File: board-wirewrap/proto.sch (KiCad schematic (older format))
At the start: 39 parts, among them P1 AB, P101 Data, P102 Power, P2 CD, SW101 RESET, U1 DS8641-LR, U101 Am2908, U102 Am2908, U103 Am2908, U104 Am2908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

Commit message: This matches the old indicator panels, the first batch before I changed them all around.
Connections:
- net +12V: now also P102.3 (P3), P102.4 (P4), P102.5 (P5), P102.6 (P6), P102.7 (P7), P102.8 (P8); no longer P102.1 (P1), P102.10 (P10), P102.2 (P2), P102.9 (P9)
- net GND: now also P102.1 (P1), P102.10 (P10), P102.2 (P2), P102.9 (P9); no longer P102.3 (P3), P102.4 (P4), P102.5 (P5), P102.6 (P6), P102.7 (P7), P102.8 (P8)
- net IPclk: now also P2.20 (D10)
- net IPdata: now also P2.22 (D11)
- net IPlatch: now also P2.24 (D12)
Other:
- note removed: "NOTES:\n\n1) Which signal goes to which package has not yet\n been fixed. Will be done during PCB layout.\n2) Do we need to tie the unconnected bus lines on\n the DS8641s to +5V?"
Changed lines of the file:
@@
 Text Label 6200 8050 2    60   ~ 0
 BDAL21
-Text Notes 3000 6750 0    60   ~ 0
-NOTES:\n\n1) Which signal goes to which package has not yet\n    been fixed. Will be done during PCB layout.\n2) Do we need to tie the unconnected bus lines on\n    the DS8641s to +5V?
 Text Label 13500 3450 3    60   ~ 0
 BDMR
@@
 L +12V #PWR128
 U 1 1 56A168EC
-P 8450 2250
-F 0 "#PWR128" H 8450 2100 50  0001 C CNN
-F 1 "+12V" H 8450 2390 50  0000 C CNN
-F 2 "" H 8450 2250 60  0000 C CNN
-F 3 "" H 8450 2250 60  0000 C CNN
-	1    8450 2250
+P 8350 2250
+F 0 "#PWR128" H 8350 2100 50  0001 C CNN
+F 1 "+12V" H 8350 2390 50  0000 C CNN
+F 2 "" H 8350 2250 60  0000 C CNN
+F 3 "" H 8350 2250 60  0000 C CNN
+	1    8350 2250
 	1    0    0    -1
 $EndComp
@@
 L +12V #PWR131
 U 1 1 56A16973
-P 9150 2250
-F 0 "#PWR131" H 9150 2100 50  0001 C CNN
-F 1 "+12V" H 9150 2390 50  0000 C CNN
-F 2 "" H 9150 2250 60  0000 C CNN
-F 3 "" H 9150 2250 60  0000 C CNN
-	1    9150 2250
+P 9250 2250
+F 0 "#PWR131" H 9250 2100 50  0001 C CNN
+F 1 "+12V" H 9250 2390 50  0000 C CNN
+F 2 "" H 9250 2250 60  0000 C CNN
+F 3 "" H 9250 2250 60  0000 C CNN
+	1    9250 2250
 	1    0    0    -1
 $EndComp
@@
 L GND #PWR127
 U 1 1 56A16A1A
-P 8350 2900
-F 0 "#PWR127" H 8350 2650 50  0001 C CNN
-F 1 "GND" H 8350 2750 50  0000 C CNN
-F 2 "" H 8350 2900 60  0000 C CNN
-F 3 "" H 8350 2900 60  0000 C CNN
-	1    8350 2900
+P 8450 2900
+F 0 "#PWR127" H 8450 2650 50  0001 C CNN
+F 1 "GND" H 8450 2750 50  0000 C CNN
+F 2 "" H 8450 2900 60  0000 C CNN
+F 3 "" H 8450 2900 60  0000 C CNN
+	1    8450 2900
 	-1   0    0    -1
 $EndComp
@@
 L GND #PWR135
 U 1 1 56A16A9A
-P 9250 2900
-F 0 "#PWR135" H 9250 2650 50  0001 C CNN
-F 1 "GND" H 9250 2750 50  0000 C CNN
-F 2 "" H 9250 2900 60  0000 C CNN
-F 3 "" H 9250 2900 60  0000 C CNN
-	1    9250 2900
-	-1   0    0    -1
-$EndComp
-Wire Wire Line
-	8450 2250 8450 2800
+P 9150 2900
+F 0 "#PWR135" H 9150 2650 50  0001 C CNN
+F 1 "GND" H 9150 2750 50  0000 C CNN
+F 2 "" H 9150 2900 60  0000 C CNN
+F 3 "" H 9150 2900 60  0000 C CNN
+	1    9150 2900
+	-1   0    0    -1
+$EndComp
 Wire Wire Line
 	8450 2800 8550 2800
 Wire Wire Line
-	8550 2400 8450 2400
-Connection ~ 8450 2400
-Wire Wire Line
 	9050 2800 9150 2800
 Wire Wire Line
-	9150 2800 9150 2250
-Wire Wire Line
-	9050 2400 9150 2400
-Connection ~ 9150 2400
-Wire Wire Line
-	9250 2900 9250 2500
+	9250 2250 9250 2700
 Wire Wire Line
 	9250 2500 9050 2500
 Wire Wire Line
-	9050 2600 9250 2600
+	9250 2600 9050 2600
 Connection ~ 9250 2600
 Wire Wire Line
-	9050 2700 9250 2700
-Connection ~ 9250 2700
-Wire Wire Line
 	8550 2500 8350 2500
 Wire Wire Line
-	8350 2500 8350 2900
-Wire Wire Line
-	8550 2600 8350 2600
+	8350 2250 8350 2700
+Wire Wire Line
+	8350 2600 8550 2600
 Connection ~ 8350 2600
-Wire Wire Line
-	8550 2700 8350 2700
-Connection ~ 8350 2700
 $Comp
 L +12V #PWR125
@@
 	1    0    0    -1
 $EndComp
+Text GLabel 11350 8100 2    60   Output ~ 0
+IPclk
+Text GLabel 11350 8200 2    60   Output ~ 0
+IPdata
+Text GLabel 11350 8300 2    60   Output ~ 0
+IPlatch
+Wire Wire Line
+	8550 2400 8450 2400
+Wire Wire Line
+	8450 2400 8450 2900
+Connection ~ 8450 2800
+Wire Wire Line
+	9050 2400 9150 2400
+Wire Wire Line
+	9150 2400 9150 2900
+Connection ~ 9150 2800
+Wire Wire Line
+	8350 2700 8550 2700
+Connection ~ 8350 2500
+Connection ~ 9250 2500
+Wire Wire Line
+	9250 2700 9050 2700
 $EndSCHEMATC

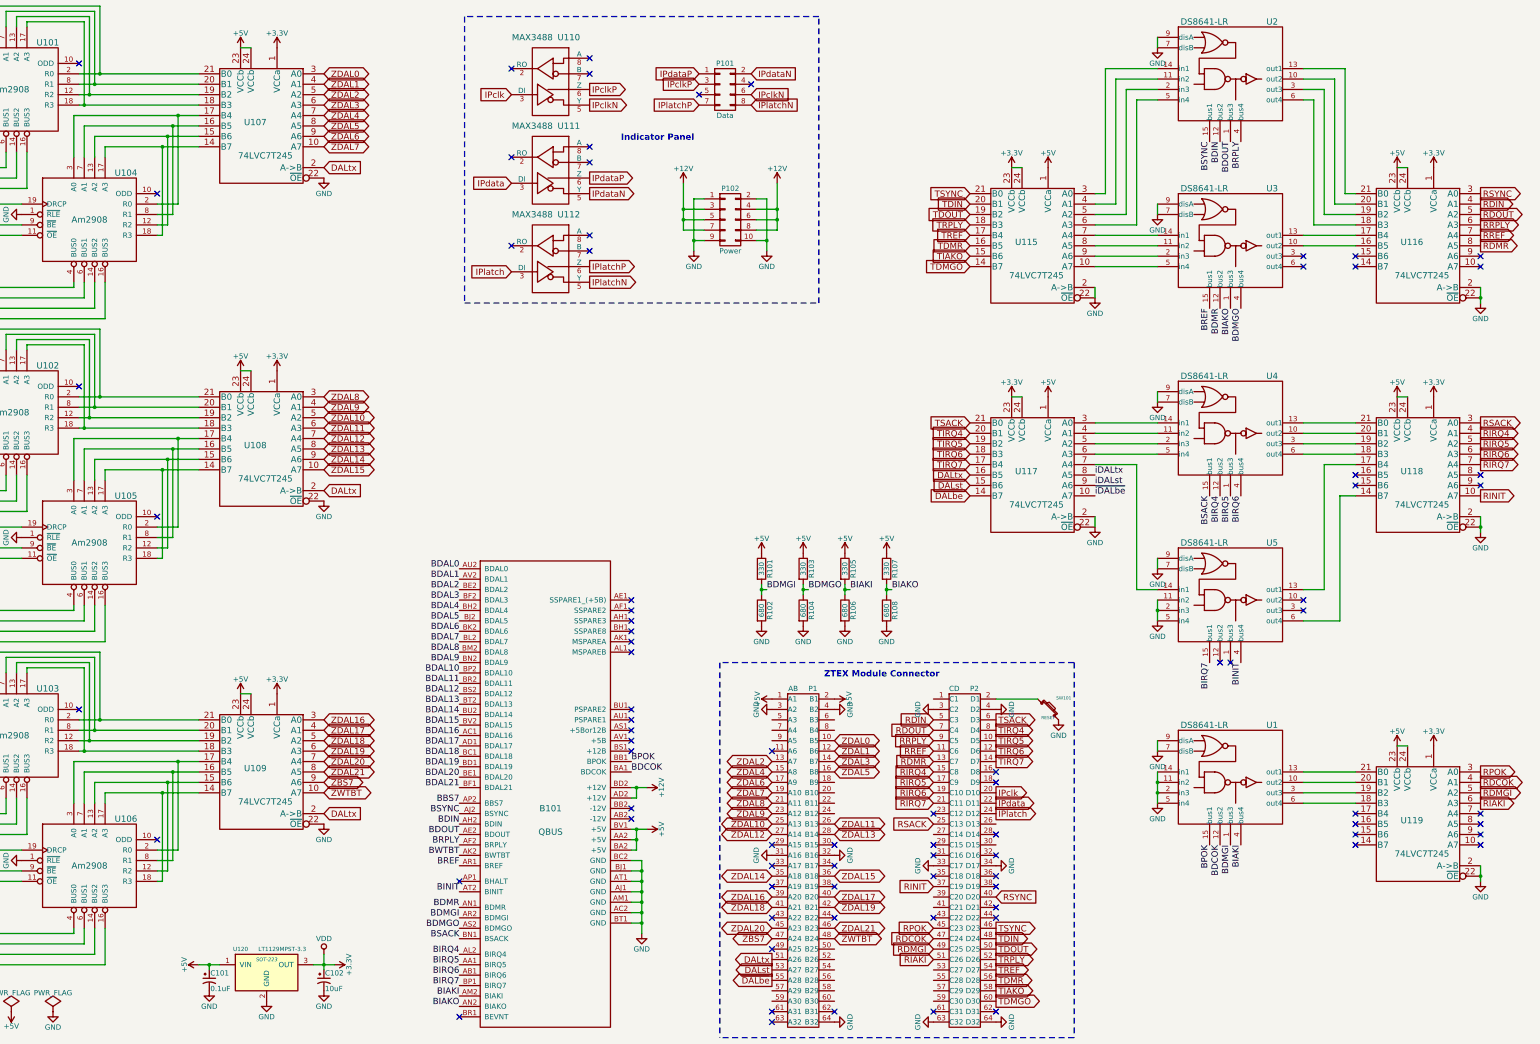
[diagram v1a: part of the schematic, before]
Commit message: Added SD card.  Not yet wired to FPGA.
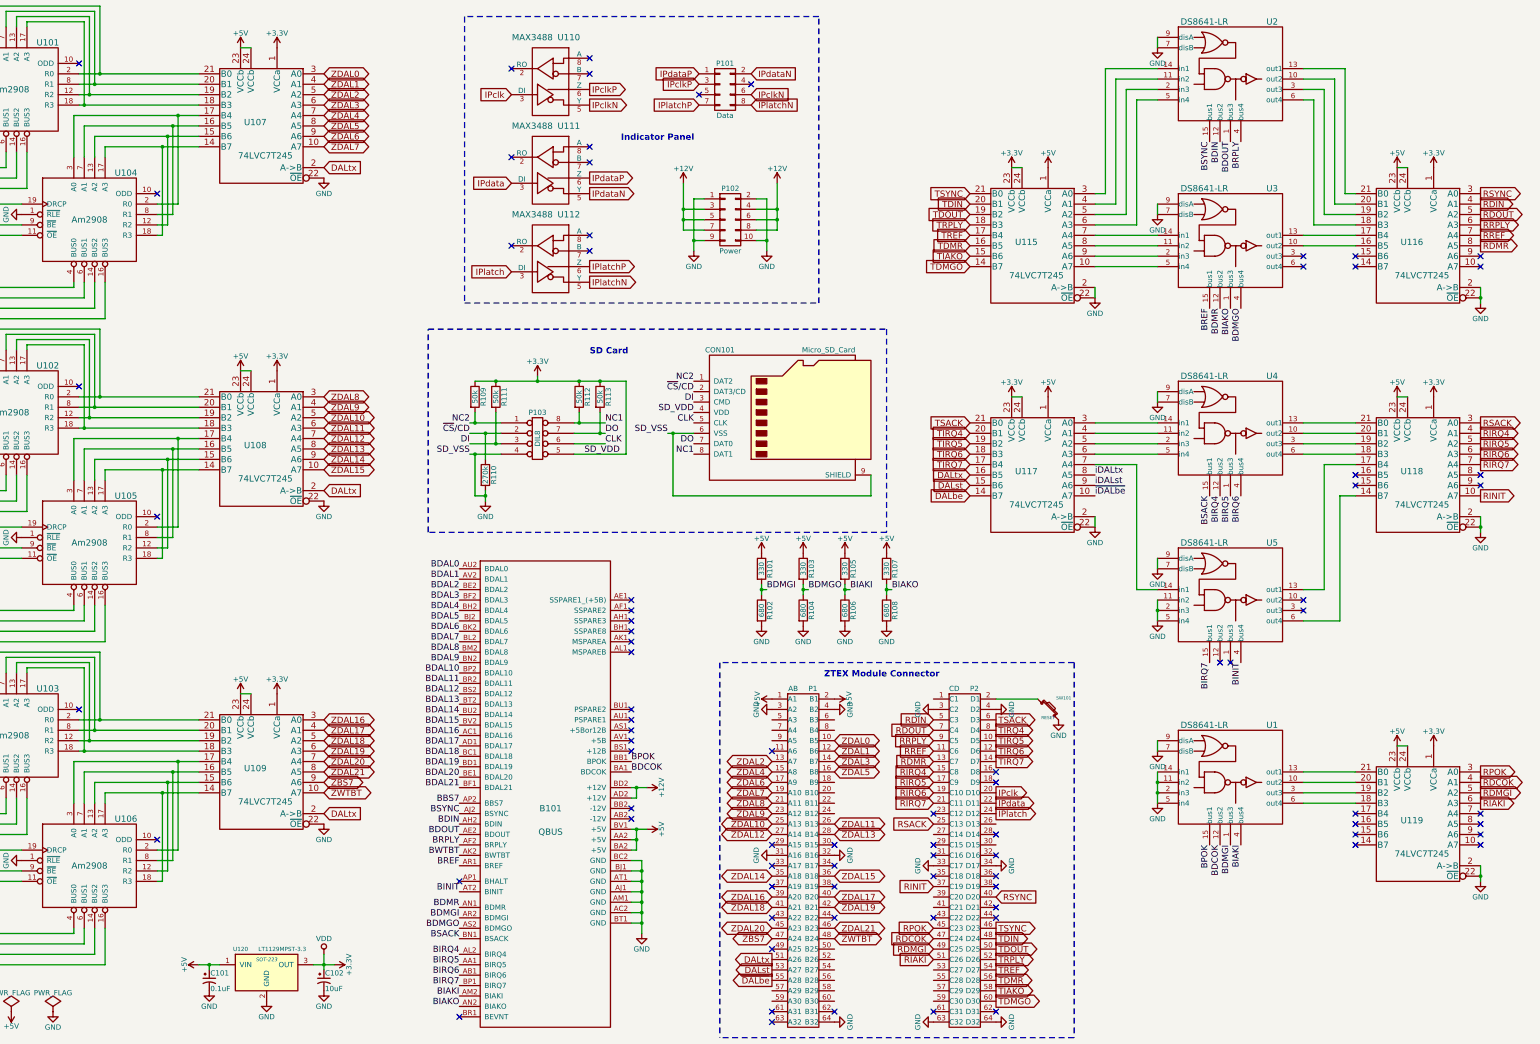
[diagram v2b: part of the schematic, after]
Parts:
- added CON101: Micro_SD_Card, symbol Micro_SD_Card
- added P103: DIL8, symbol DIL8
- added R109, R111, R112, R113: 50k, symbol R
- added R110: 270k, symbol R
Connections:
- net +3V3: now also CON101.4 (VDD), P103.5 (P5), R109.1, R111.1, R112.1, R113.1
- net GND: now also CON101.6 (VSS), CON101.9 (SHIELD), P103.4 (P4), R110.2
- new net CLK: CON101.5 (CLK), P103.6 (P6)
- new net DI: CON101.3 (CMD), P103.3 (P3), R111.2
- new net DO: CON101.7 (DAT0), P103.7 (P7), R113.2
- new net NC1: CON101.8 (DAT1), P103.8 (P8), R112.2
- new net NC2: CON101.1 (DAT2), P103.1 (P1), R109.2
- new net ~CS~/CD: CON101.2 (DAT3/CD), P103.2 (P2), R110.1
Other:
- note added: "SD Card"

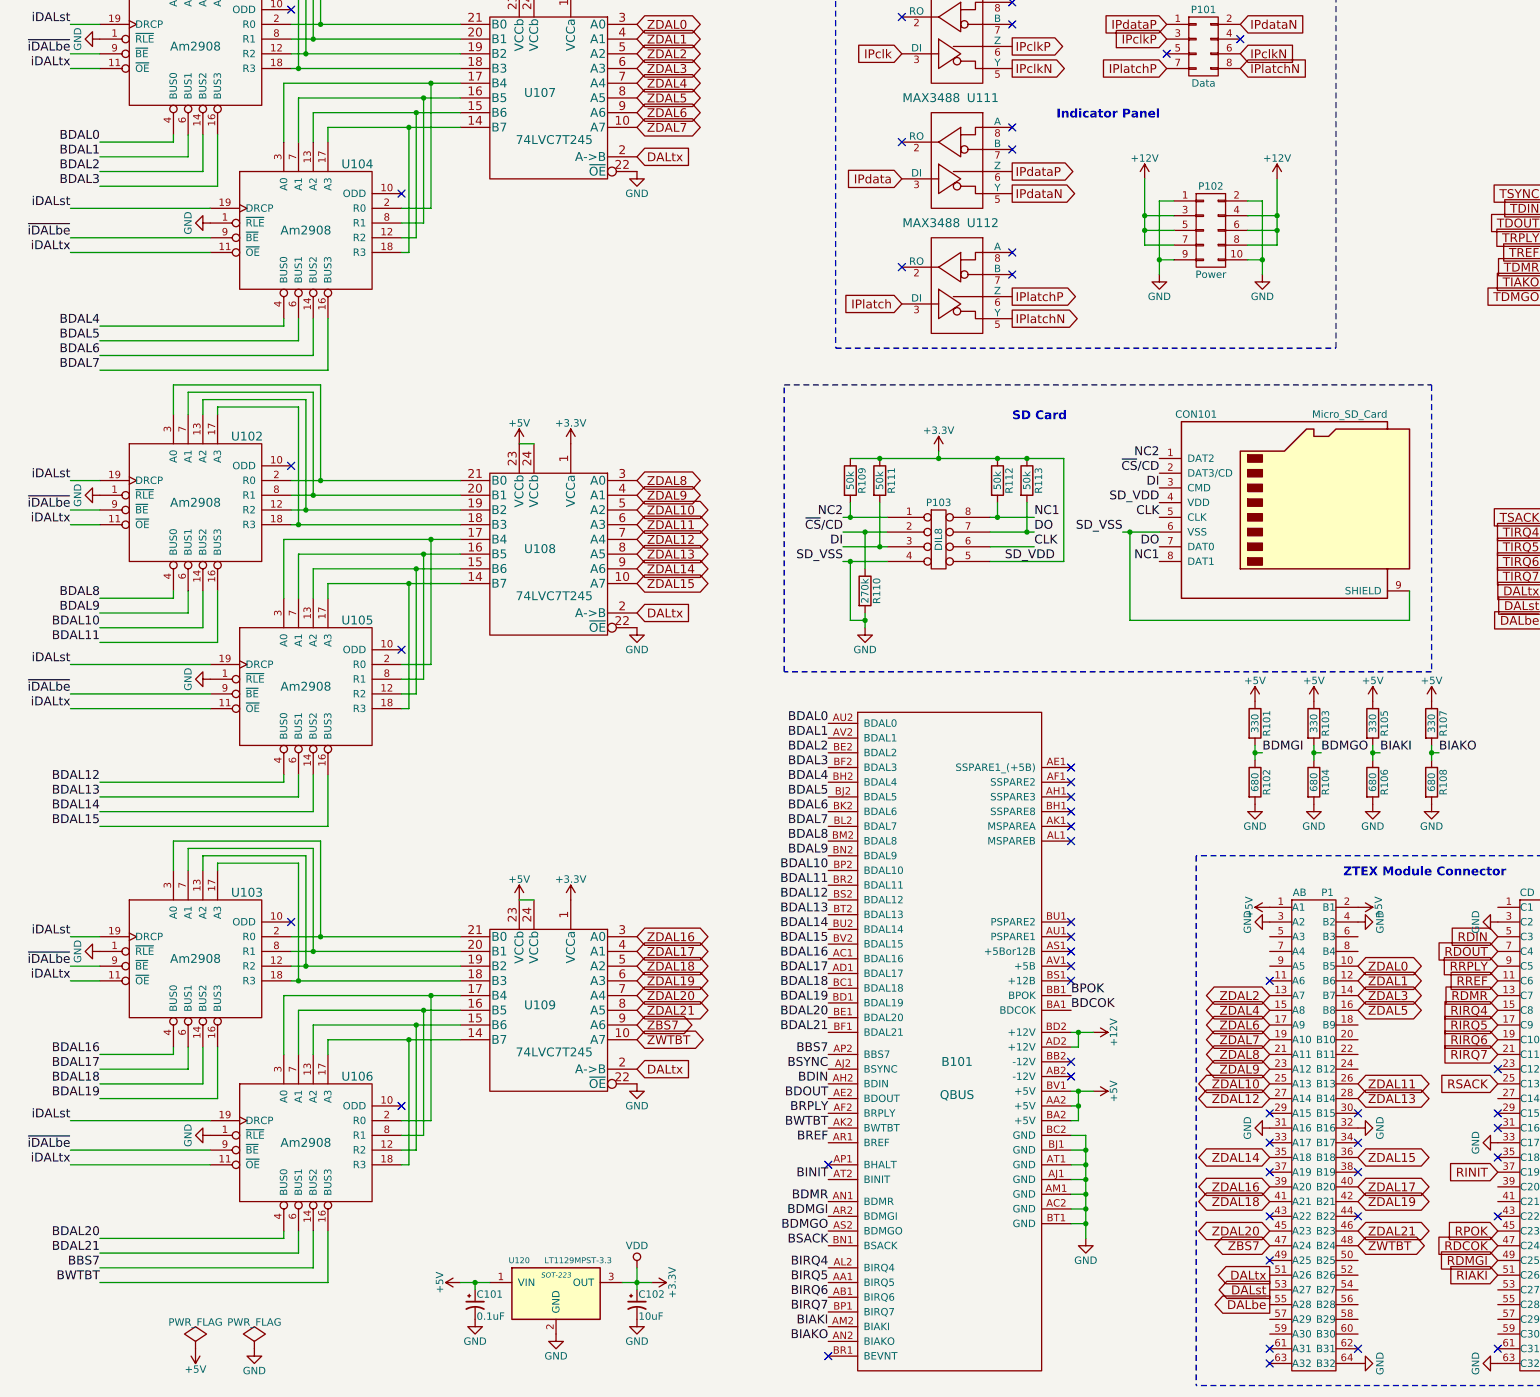
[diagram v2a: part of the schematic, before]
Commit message: Attached SD card to FPGA.
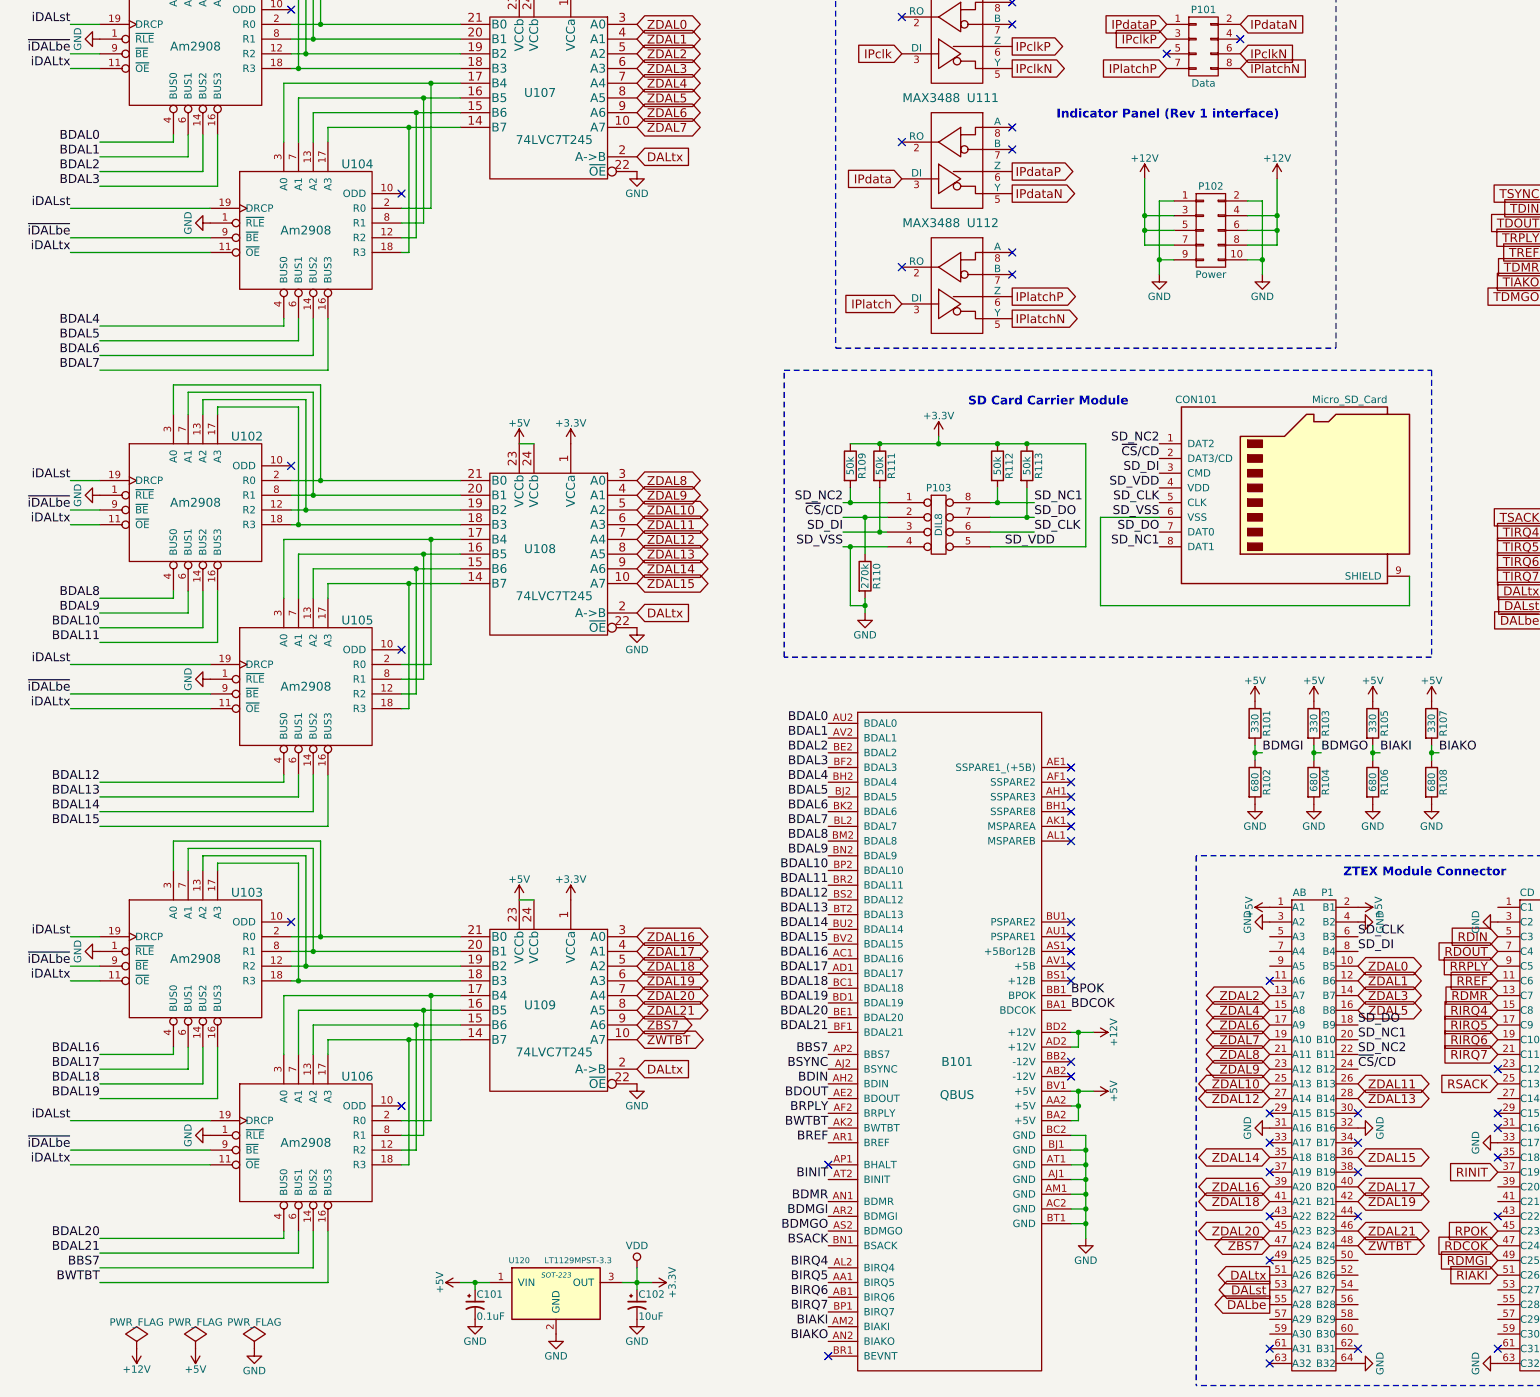
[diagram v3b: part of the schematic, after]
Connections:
- net CLK is gone; now on net SD_CLK: CON101.5 (CLK), P103.6 (P6)
- net DI is gone; now on net SD_DI: CON101.3 (CMD), P103.3 (P3), R111.2
- net DO is gone; now on net SD_DO: CON101.7 (DAT0), P103.7 (P7), R113.2
- net NC1 is gone; now on net SD_NC1: CON101.8 (DAT1), P103.8 (P8), R112.2
- net NC2 is gone; now on net SD_NC2: CON101.1 (DAT2), P103.1 (P1), R109.2
- net ~CS~/CD: now also P1.24 (B12)
- net SD_DO: now reaches P1.18 (B9)
- net SD_NC1: now reaches P1.20 (B10)
- net SD_NC2: now reaches P1.22 (B11)
- net SD_CLK: now reaches P1.6 (B3)
- net SD_DI: now reaches P1.8 (B4)
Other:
- note added: "Indicator Panel (Rev 1 interface)"
- note added: "SD Card Carrier Module"
- note removed: "Indicator Panel"
- note removed: "SD Card"
- moved on the sheet: CON101, P103, R109, R110, R111, R112, R113
